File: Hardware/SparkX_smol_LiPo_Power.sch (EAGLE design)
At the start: 40 parts, among them J3 AVR_SPI_PROG_3X2TESTPOINTS, Q1 3.1A/30V/105mΩ, U1 STLQ015-3.3V, U2 MCP73831, U3 3.3V, U4 MAX17048, U5 ATTINY841-ARDUINO_QFN20M1

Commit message: Update smol symbol
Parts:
- added U$3, U$9: SMOL_LOGOSMALL, SparkX:SMOL_LOGOSMALL
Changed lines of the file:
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@@
 <part name="C7" library="SparkFun-Capacitors" deviceset="2.2UF" device="-0402_TIGHT-10V-10%-X5R" value="2.2uF"/>
 <part name="GND9" library="SparkFun-PowerSymbols" deviceset="GND" device=""/>
+<part name="U$3" library="SparkX" deviceset="SMOL_LOGO" device="SMALL"/>
+<part name="U$9" library="SparkX" deviceset="SMOL_LOGO" device="SMALL"/>
 </parts>
 <sheets>
@@
 <attribute name="VALUE" x="220.98" y="136.906" size="1.778" layer="96" font="vector" align="top-center"/>
 </instance>
+<instance part="U$3" gate="G$1" x="307.34" y="40.64" smashed="yes"/>
+<instance part="U$9" gate="G$1" x="307.34" y="40.64" smashed="yes"/>
 </instances>
 <busses>

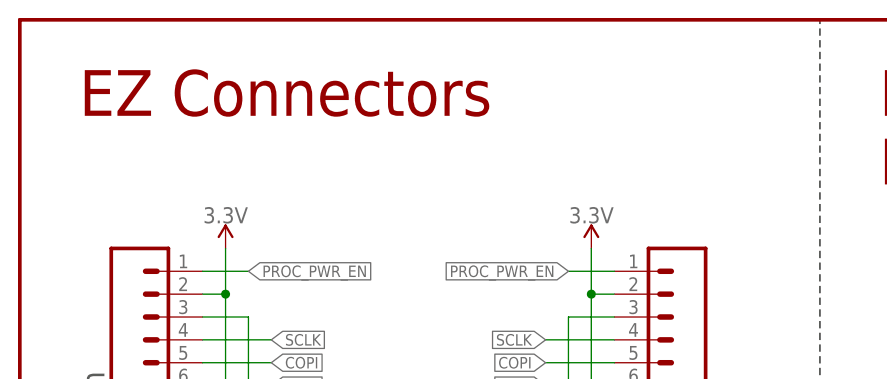
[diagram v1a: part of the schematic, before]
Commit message: Change EZ to smôl on schematic
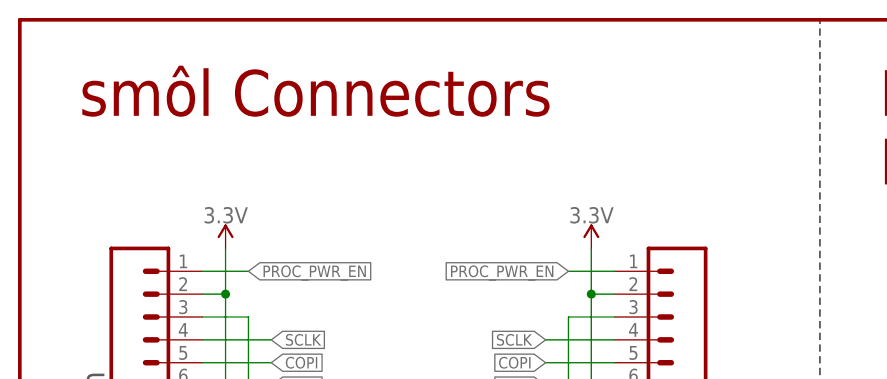
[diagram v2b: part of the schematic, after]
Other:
- note added: "smôl Connectors"
- note removed: "EZ Connectors"
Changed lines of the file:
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@@
 <wire x1="88.9" y1="190.5" x2="88.9" y2="279.4" width="0.2032" layer="97" style="longdash"/>
 <wire x1="88.9" y1="190.5" x2="0" y2="190.5" width="0.2032" layer="97" style="longdash"/>
-<text x="6.604" y="268.732" size="5.08" layer="94">EZ Connectors</text>
+<text x="6.604" y="268.732" size="5.08" layer="94">smôl Connectors</text>
 <text x="76.962" y="236.22" size="2.54" layer="97" font="vector" rot="R270">Top</text>
 <text x="9.398" y="228.854" size="2.54" layer="97" font="vector" rot="R90">Bottom</text>
